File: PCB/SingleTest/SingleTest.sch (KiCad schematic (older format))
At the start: 1 part

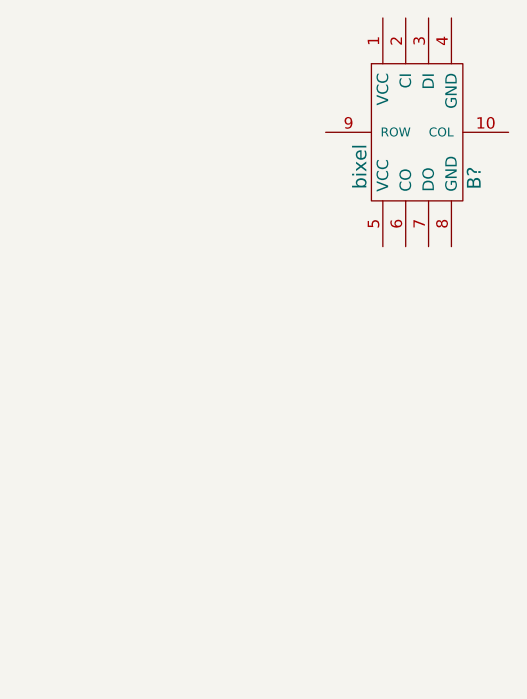
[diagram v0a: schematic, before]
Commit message: Adding single test
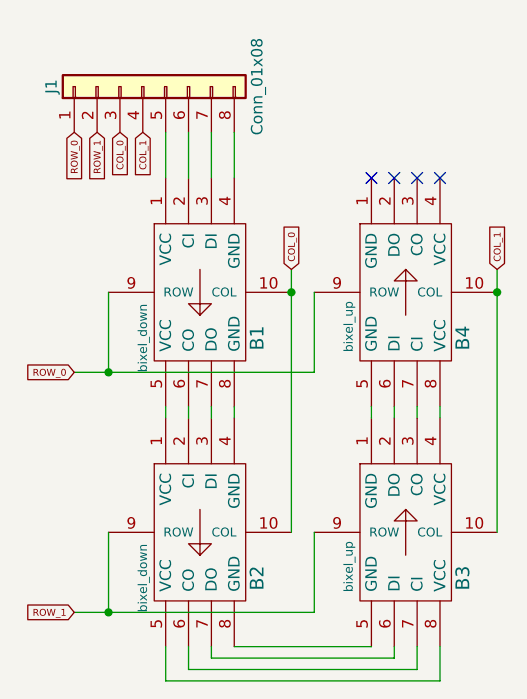
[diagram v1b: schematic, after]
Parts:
- removed B?: bixel, symbol bixel
- added B1, B2: bixel_down, symbol bixel_down
- added B3, B4: bixel_up, symbol bixel_up
- added J1: Conn_01x08, symbol Conn_01x08
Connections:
- new net: B1.1 (VCC), J1.5 (Pin_5)
- new net: B1.2 (CI), J1.6 (Pin_6)
- new net: B1.3 (DI), J1.7 (Pin_7)
- new net: B1.4 (GND), J1.8 (Pin_8)
- new net: B1.5 (VCC), B2.1 (VCC)
- new net: B1.6 (CO), B2.2 (CI)
- new net: B1.7 (DO), B2.3 (DI)
- new net: B1.8 (GND), B2.4 (GND)
- new net: B3.1 (GND), B4.5 (GND)
- new net: B3.2 (DO), B4.6 (DI)
- new net: B3.3 (CO), B4.7 (CI)
- new net: B3.4 (VCC), B4.8 (VCC)
- new net: B2.5 (VCC), B3.8 (VCC)
- new net: B2.6 (CO), B3.7 (CI)
- new net: B2.7 (DO), B3.6 (DI)
- new net: B2.8 (GND), B3.5 (GND)
- new net COL_0: B1.10 (COL), B2.10 (COL), J1.3 (Pin_3)
- new net COL_1: B3.10 (COL), B4.10 (COL), J1.4 (Pin_4)
- new net ROW_0: B1.9 (ROW), B4.9 (ROW), J1.1 (Pin_1)
- new net ROW_1: B2.9 (ROW), B3.9 (ROW), J1.2 (Pin_2)
- no-connect marks 0 -> 4
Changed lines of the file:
@@
 $EndDescr
 $Comp
-L bixel B?
-U 1 1 5B35672E
-P 3550 2700
-F 0 "B?" V 3800 2500 60  0000 C CNN
-F 1 "bixel" V 3300 2550 60  0000 C CNN
-F 2 "" H 3550 2700 60  0001 C CNN
-F 3 "" H 3550 2700 60  0001 C CNN
-	1    3550 2700
+L bixel_down B1
+U 1 1 5B36BF26
+P 2600 3400
+F 0 "B1" V 2850 3200 60  0000 C CNN
+F 1 "bixel_down" V 2350 3200 39  0000 C CNN
+F 2 "" H 2600 3400 60  0001 C CNN
+F 3 "" H 2600 3400 60  0001 C CNN
+	1    2600 3400
 	1    0    0    -1
 $EndComp
+$Comp
+L bixel_up B4
+U 1 1 5B36BF6D
+P 3500 3400
+F 0 "B4" V 3750 3200 60  0000 C CNN
+F 1 "bixel_up" V 3250 3250 39  0000 C CNN
+F 2 "" H 3500 3400 60  0001 C CNN
+F 3 "" H 3500 3400 60  0001 C CNN
+	1    3500 3400
+	1    0    0    -1
+$EndComp
+$Comp
+L bixel_down B2
+U 1 1 5B36BFAC
+P 2600 4450
+F 0 "B2" V 2850 4250 60  0000 C CNN
+F 1 "bixel_down" V 2350 4250 39  0000 C CNN
+F 2 "" H 2600 4450 60  0001 C CNN
+F 3 "" H 2600 4450 60  0001 C CNN
+	1    2600 4450
+	1    0    0    -1
+$EndComp
+$Comp
+L bixel_up B3
+U 1 1 5B36BFD9
+P 3500 4450
+F 0 "B3" V 3750 4250 60  0000 C CNN
+F 1 "bixel_up" V 3250 4300 39  0000 C CNN
+F 2 "" H 3500 4450 60  0001 C CNN
+F 3 "" H 3500 4450 60  0001 C CNN
+	1    3500 4450
+	1    0    0    -1
+$EndComp
+Wire Wire Line
+	2450 3900 2450 3950
+Wire Wire Line
+	2550 3950 2550 3900
+Wire Wire Line
+	2650 3900 2650 3950
+Wire Wire Line
+	2750 3950 2750 3900
+Wire Wire Line
+	3350 3900 3350 3950
+Wire Wire Line
+	3450 3950 3450 3900
+Wire Wire Line
+	3550 3900 3550 3950
+Wire Wire Line
+	3650 3950 3650 3900
+Wire Wire Line
+	2750 4950 3350 4950
+Wire Wire Line
+	2650 4950 2650 5000
+Wire Wire Line
+	2650 5000 3450 5000
+Wire Wire Line
+	3450 5000 3450 4950
+Wire Wire Line
+	2550 4950 2550 5050
+Wire Wire Line
+	2550 5050 3550 5050
+Wire Wire Line
+	3550 5050 3550 4950
+Wire Wire Line
+	2450 4950 2450 5100
+Wire Wire Line
+	2450 5100 3650 5100
+Wire Wire Line
+	3650 5100 3650 4950
+Wire Wire Line
+	3000 3300 3000 4450
+Wire Wire Line
+	3900 3300 3900 4450
+Wire Wire Line
+	3100 3400 3100 3750
+Wire Wire Line
+	3100 3750 2050 3750
+Wire Wire Line
+	2200 3400 2200 3750
+Connection ~ 2200 3750
+Wire Wire Line
+	3100 4450 3100 4800
+Wire Wire Line
+	3100 4800 2050 4800
+Wire Wire Line
+	2200 4450 2200 4800
+Connection ~ 2200 4800
+NoConn ~ 3350 2900
+NoConn ~ 3450 2900
+NoConn ~ 3550 2900
+NoConn ~ 3650 2900
+$Comp
+L Conn_01x08 J1
+U 1 1 5B36C3AB
+P 2350 2500
+F 0 "J1" H 2350 2900 50  0000 C CNN
+F 1 "Conn_01x08" H 2350 2000 50  0000 C CNN
+F 2 "" H 2350 2500 50  0001 C CNN
+F 3 "" H 2350 2500 50  0001 C CNN
+	1    2350 2500
+	0    -1   -1   0
+$EndComp
+Text GLabel 2050 3750 0    30   Input ~ 0
+ROW_0
+Text GLabel 2050 4800 0    30   Input ~ 0
+ROW_1
+Text GLabel 3000 3300 1    30   Input ~ 0
+COL_0
+Text GLabel 3900 3300 1    30   Input ~ 0
+COL_1
+Connection ~ 3000 3400
+Connection ~ 3900 3400
+Wire Wire Line
+	2450 2700 2450 2900
+Wire Wire Line
+	2550 2900 2550 2700
+Wire Wire Line
+	2650 2700 2650 2900
+Wire Wire Line
+	2750 2900 2750 2700
+Text GLabel 2050 2700 3    30   Input ~ 0
+ROW_0
+Text GLabel 2150 2700 3    30   Input ~ 0
+ROW_1
+Text GLabel 2250 2700 3    30   Input ~ 0
+COL_0
+Text GLabel 2350 2700 3    30   Input ~ 0
+COL_1
 $EndSCHEMATC

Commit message: tweaks
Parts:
- B1, B2, B3, B4: footprint (none) -> custom:bixel
- J1: footprint (none) -> Socket_Strips:Socket_Strip_Straight_1x08_Pitch2.54mm
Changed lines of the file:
@@
 F 0 "B1" V 2850 3200 60  0000 C CNN
 F 1 "bixel_down" V 2350 3200 39  0000 C CNN
-F 2 "" H 2600 3400 60  0001 C CNN
+F 2 "custom:bixel" H 2600 3400 60  0001 C CNN
 F 3 "" H 2600 3400 60  0001 C CNN
 	1    2600 3400
@@
 F 0 "B4" V 3750 3200 60  0000 C CNN
 F 1 "bixel_up" V 3250 3250 39  0000 C CNN
-F 2 "" H 3500 3400 60  0001 C CNN
+F 2 "custom:bixel" H 3500 3400 60  0001 C CNN
 F 3 "" H 3500 3400 60  0001 C CNN
 	1    3500 3400
@@
 F 0 "B2" V 2850 4250 60  0000 C CNN
 F 1 "bixel_down" V 2350 4250 39  0000 C CNN
-F 2 "" H 2600 4450 60  0001 C CNN
+F 2 "custom:bixel" H 2600 4450 60  0001 C CNN
 F 3 "" H 2600 4450 60  0001 C CNN
 	1    2600 4450
@@
 F 0 "B3" V 3750 4250 60  0000 C CNN
 F 1 "bixel_up" V 3250 4300 39  0000 C CNN
-F 2 "" H 3500 4450 60  0001 C CNN
+F 2 "custom:bixel" H 3500 4450 60  0001 C CNN
 F 3 "" H 3500 4450 60  0001 C CNN
 	1    3500 4450
@@
 F 0 "J1" H 2350 2900 50  0000 C CNN
 F 1 "Conn_01x08" H 2350 2000 50  0000 C CNN
-F 2 "" H 2350 2500 50  0001 C CNN
+F 2 "Socket_Strips:Socket_Strip_Straight_1x08_Pitch2.54mm" H 2350 2500 50  0001 C CNN
 F 3 "" H 2350 2500 50  0001 C CNN
 	1    2350 2500
